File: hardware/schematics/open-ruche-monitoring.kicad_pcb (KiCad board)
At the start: 2 copper layers, 139.4 x 98.4 mm, 31 parts, among them J1 HX711, J10 MMA8451, J11 CONN_LIPO, J12 CONN_ALIM_ESP32, J2 DHT22_EXT, J3 DHT22_INT, J4 SONDE_TEMP_1, J5 SONDE_TEMP_2, J6 Light Sensor, J7 LORA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

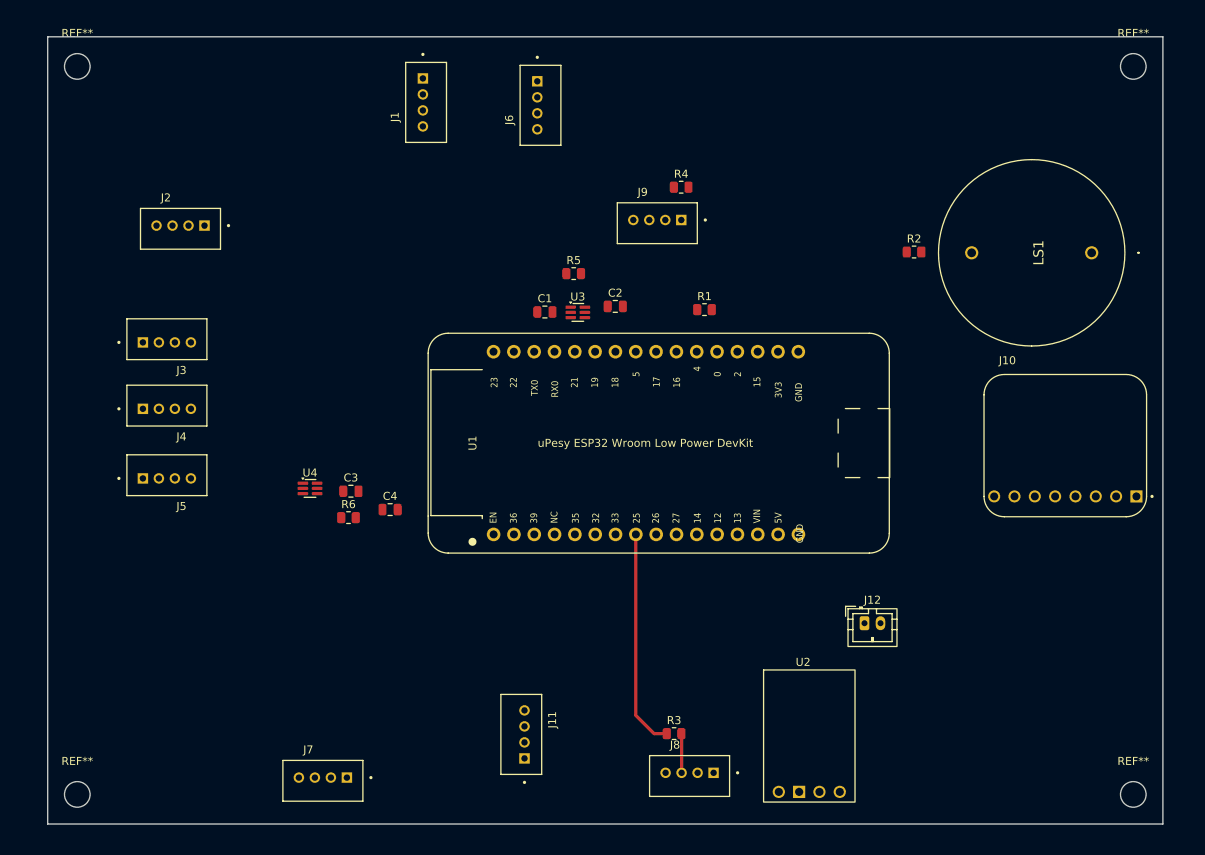
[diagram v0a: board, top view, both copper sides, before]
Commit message: hw(3D) Add 3D models for lora, hx711 and lipo charger
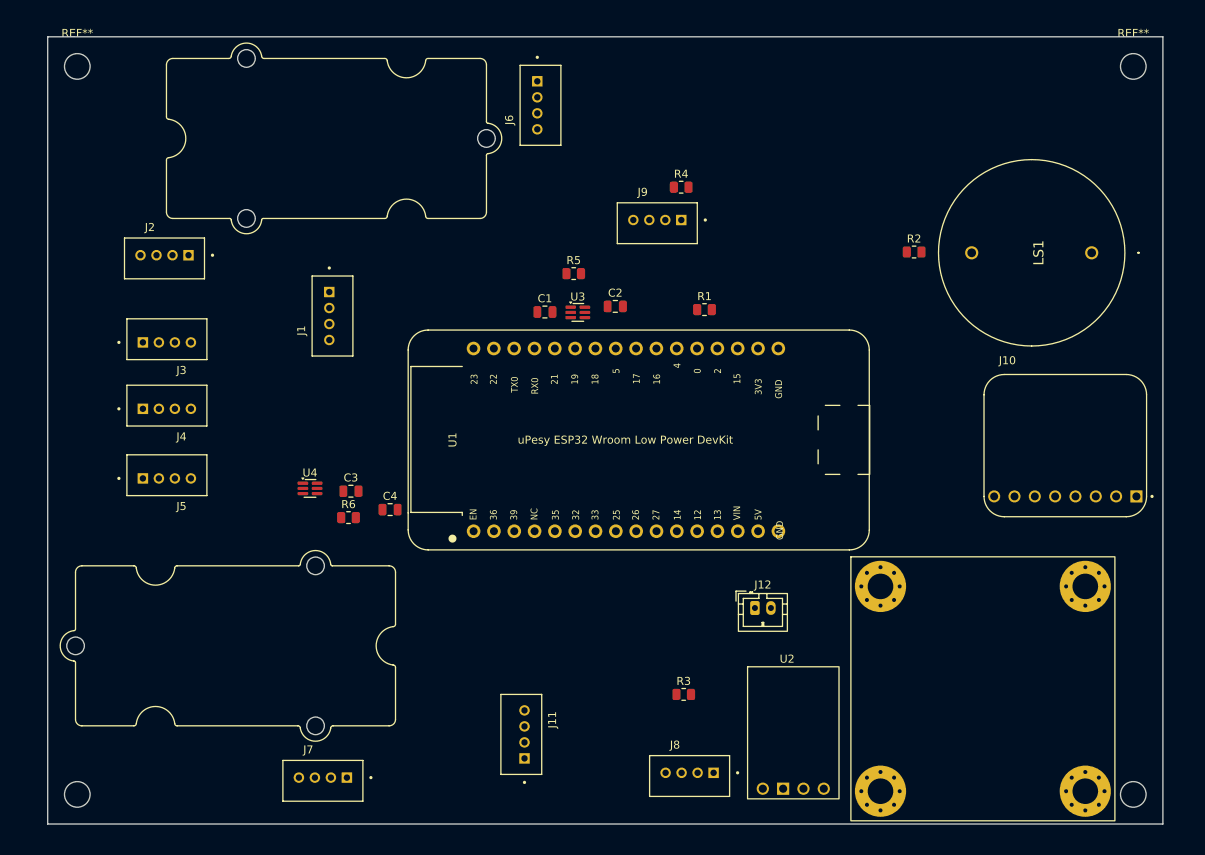
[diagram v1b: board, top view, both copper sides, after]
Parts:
- added REF**: DFR0264, lipo_charger:DFR0264, F.Cu at (197.9, 125.9)
- added REF**: hx711_module, hx711_grove:hx711_module, F.Cu at (98.5, 55.7)
- added REF**: lora_module, lora_grove:lora_module, F.Cu at (105.5, 126.8)
- U1: value uPesy_ESP32_Wroom_Low_Power_DevKit -> uPesy ESP32 Wroom Low Power DevKit
- moved J1 29.2 mm to (117.0, 77.9)
- moved J12 13.8 mm to (170.2, 114.4)
- moved R3 5.04 mm to (161.3, 125.2)
- moved J2 4.21 mm to (96.4, 70.3)
- moved U1 2.53 mm to (154.0, 93.5)
- moved U2 2.04 mm to (175.0, 130.0)
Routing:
- net /TX_XIAO: track 27.4 -> 0.00 mm
- net Net-(J8-SIG1): track 4.91 -> 0.00 mm

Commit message: hw(pcb) save pcb to try another layout
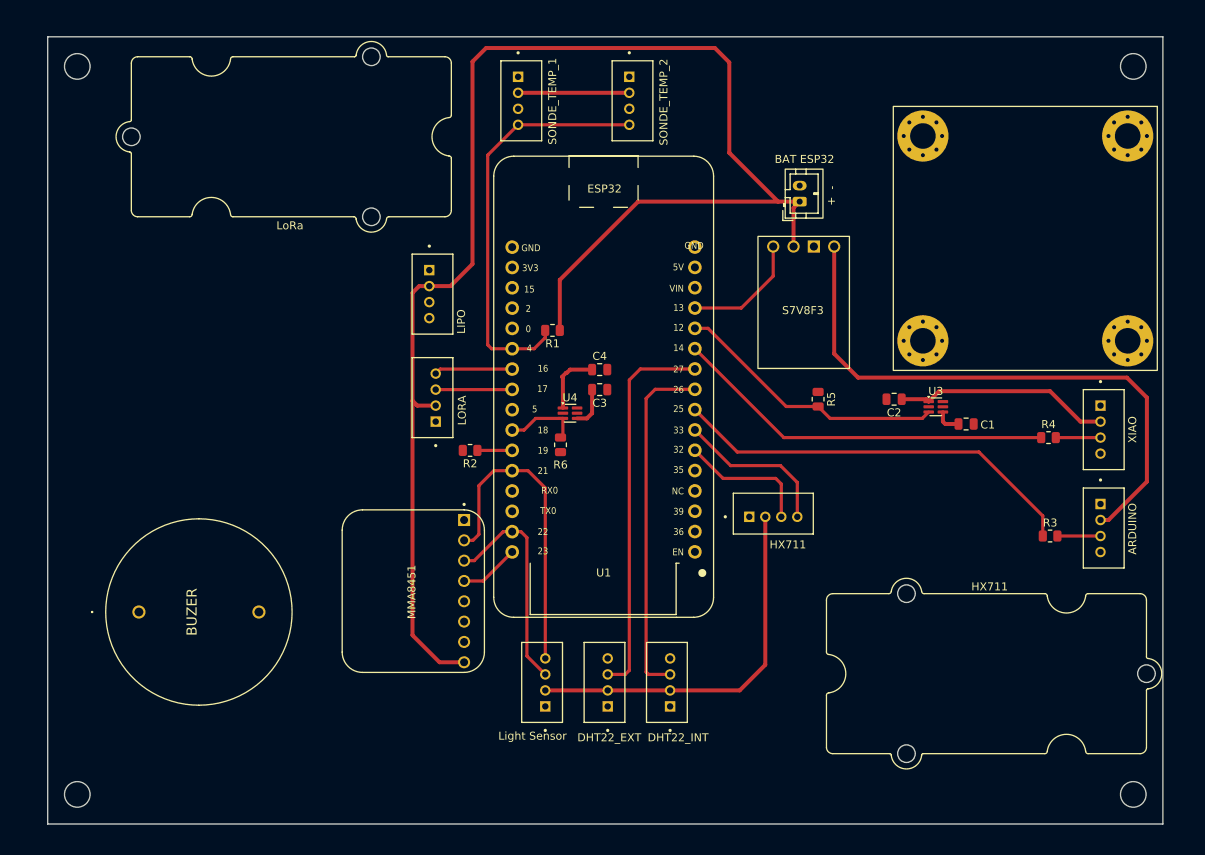
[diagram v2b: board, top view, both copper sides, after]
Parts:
- BAT ESP32: renamed from J12
- J11: value CONN_LIPO -> LIPO
- REF**: value lora_module -> LoRa
- U1: value uPesy ESP32 Wroom Low Power DevKit -> uPesy_ESP32_Wroom_Low_Power_DevKit
- U2: value 3.3V-STEP-DOWN_VOLTAGE_REGULATOR_S7V8F3 -> S7V8F3
- moved BUZER 127.3 mm to (93.2, 114.9), turned to -90 degrees
- moved REF** 106.2 mm to (181.0, 122.6)
- moved J10 83.5 mm to (127.5, 112.3), turned to 90 degrees
- moved J2 76.9 mm to (151.8, 123.7), turned to -90 degrees
- moved J3 75.9 mm to (159.6, 123.7), turned to -90 degrees
- moved J5 74.6 mm to (154.5, 51.0), turned to 90 degrees
- moved J6 72.1 mm to (144.0, 123.7), turned to -90 degrees
- moved REF** 64.0 mm to (112.5, 63.2)
- moved XIAO 61.3 mm to (213.4, 92.1), turned to 90 degrees
- moved HX711 60.9 mm to (172.5, 103.0), turned to 180 degrees
- moved R2 60.8 mm to (134.6, 94.7), turned to 180 degrees
- moved ARDUINO 59.8 mm to (213.4, 104.4), turned to 90 degrees
- moved REF** 58.7 mm to (202.6, 67.4), turned to -90 degrees
- moved J4 58.4 mm to (140.6, 51.0), turned to 90 degrees
- moved J11 56.3 mm to (129.5, 75.2), turned to 90 degrees
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- renumbered J8 to ARDUINO, LS1 to BUZER, J1 to HX711, J9 to XIAO
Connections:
- U1 pad 12: /EN_SENSORS -> /EN_XIAO
- U1 pad 23: /EN_XIAO -> /EN_SENSORS
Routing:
- net /+3.7V: track 0.00 -> 196.2 mm
- net /LS_ARDUINO_OUT: track 0.00 -> 73.0 mm
- net /LS_SENSORS_OUT: track 0.00 -> 69.3 mm
- net /ONE_WIRE_TEMP: track 0.00 -> 51.8 mm
- net /TX_XIAO: track 0.00 -> 51.5 mm
- net /DATA_DHT22_EXT: track 0.00 -> 48.0 mm
- net /TX_ARDUINO: track 0.00 -> 47.9 mm
- net /DATA_DHT22_INT: track 0.11 -> 44.0 mm
- net /SDA: track 0.00 -> 39.5 mm
- net /EN_XIAO: track 0.00 -> 34.2 mm
- net /SCL: track 0.00 -> 27.7 mm
- net /LS_XIAO_OUT: track 0.00 -> 27.1 mm
- net /PSCK: track 0.00 -> 19.8 mm
- net /DOUT: track 0.00 -> 16.6 mm
- net /EN_ARDUINO: track 0.00 -> 15.1 mm
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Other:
- board text added: "+"
- board text added: "-"

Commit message: hw(pcb) pcb done
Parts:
- removed ARDUINO: CONN_ARDUINO, Grove:SEEED_110990030
- removed BAT ESP32: CONN_ALIM_ESP32, Connector_JST:JST_PH_B2B-PH-K_1x02_P2.00mm_Vertical
- removed BUZER: KPEG222, KPEG222:KPEG222
- removed C1, C3: 1u, Capacitor_SMD:C_0805_2012Metric
- removed C2, C4: 0.1u, Capacitor_SMD:C_0805_2012Metric
- removed HX711: HX711, Grove:SEEED_110990030
- removed R5, R6: 20k, Resistor_SMD:R_0805_2012Metric
- removed the REF** at (202.6, 67.4)
- removed the REF** at (112.5, 63.2)
- removed U4: SiP32431DR3, Package_TO_SOT_SMD:SOT-363_SC-70-6
- removed XIAO: CONN_XIAO, Grove:SEEED_110990030
- added BAT: lipo_bat, battery:lipo_bat, F.Cu at (106.3, 95.9)
- added BUZZER: KPEG222, KPEG222:KPEG222, F.Cu at (213.4, 93.9)
- added J1: HX711, Grove:SEEED_110990030, F.Cu at (156.9, 64.3)
- added J12: BAT ESP32, Connector_JST:JST_PH_B2B-PH-K_1x02_P2.00mm_Vertical, F.Cu at (125.4, 60.2)
- added J8: ARDUINO, Grove:SEEED_110990030, F.Cu at (182.6, 75.4)
- added J9: XIAO, Grove:SEEED_110990030, F.Cu at (189.0, 75.3)
- added LIPO_CHARGER: LIPO CHARGER, lipo_charger:DFR0264, F.Cu at (103.9, 67.0)
- added LORA: lora_module, lora_grove:lora_module, F.Cu at (198.8, 113.3)
- J11: value LIPO -> CONN ALIM
- J6: value Light Sensor -> LUX
- R1, R2, R3, R4: footprint Resistor_SMD:R_0805_2012Metric -> Resistor_THT:R_Axial_DIN0207_L6.3mm_D2.5mm_P10.16mm_Horizontal
- U1: value uPesy_ESP32_Wroom_Low_Power_DevKit -> uPesy ESP32 Wroom Low Power DevKit
- U3: value SiP32431DR3 -> S7V8F5; footprint Package_TO_SOT_SMD:SOT-363_SC-70-6 -> Pololu:MODULE_STEP-DOWN_VOLTAGE_REGULATOR_D24V6F3
- moved R3 67.5 mm to (145.7, 77.2)
- moved REF** 67.1 mm to (174.4, 55.8)
- moved J5 64.0 mm to (133.1, 111.3), turned to -90 degrees
- moved J4 60.3 mm to (141.8, 111.3), turned to -90 degrees
- moved J3 60.1 mm to (150.5, 64.3), turned to 90 degrees
- moved J2 59.9 mm to (143.8, 64.3), turned to 90 degrees
- moved U3 57.6 mm to (150.4, 50.3), turned to -90 degrees
- moved R4 54.9 mm to (153.5, 80.4)
- moved R2 46.8 mm to (181.3, 92.1), turned to 0 degrees
- moved U2 43.9 mm to (135.1, 61.1)
- moved J10 40.0 mm to (167.2, 107.2), turned to 180 degrees
- moved J7 30.8 mm to (150.6, 111.3)
- moved J11 26.6 mm to (125.1, 48.9), turned to 0 degrees
- moved R1 22.0 mm to (135.6, 99.6), turned to 0 degrees
- moved J6 18.5 mm to (161.9, 119.2), turned to 0 degrees
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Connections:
- J10 pad 1: GND -> unconnected-(J10-Pin_1-Pad1)
- J10 pad 8: /+3.7V -> /+3.3V
- J2 pad 2: /LS_SENSORS_OUT -> /+3.3V_REG
- J3 pad 2: /LS_SENSORS_OUT -> /+3.3V_REG
- J4 pad 2: /LS_SENSORS_OUT -> /+3.3V_REG
- J5 pad 2: /LS_SENSORS_OUT -> /+3.3V_REG
- J6 pad 2: /LS_SENSORS_OUT -> /+3.3V_REG
- J7 pad 2: /+3.7V -> /+3.3V_REG
- R1 pad 1: /+3.7V -> /+3.3V
- R3 pad 1: /TX_XIAO -> /TX_ARDUINO
- R4 pad 1: /TX_ARDUINO -> /TX_XIAO
- U1 pad 12: /EN_XIAO -> /EN_3.3V_REG
- U1 pad 13: /EN_ARDUINO -> /EN_5V_REG
- U1 pad 23: /EN_SENSORS -> unconnected-(U1-GPIO18-Pad23)
- U1 pad 31: unconnected-(U1-3V3-Pad31) -> /+3.3V
- U2 pad !SHDN: /EN_ARDUINO -> /EN_3.3V_REG
- U2 pad VOUT: /LS_ARDUINO_OUT -> /+3.3V_REG
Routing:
- net /+3.7V: track 196.2 -> 32.4 mm
- net /+3.3V_REG: track 0.00 -> 130.5 mm, vias 0 -> 1
- net /LS_ARDUINO_OUT: track 73.0 -> 0.00 mm
- net /+3.3V: track 0.00 -> 72.3 mm
- net /LS_SENSORS_OUT: track 69.3 -> 0.00 mm
- net /+5V_REG: track 0.00 -> 57.2 mm
- net /TX_XIAO: track 51.5 -> 8.01 mm
- net /TX_ARDUINO: track 47.9 -> 4.73 mm
- net /DATA_DHT22_EXT: track 48.0 -> 9.01 mm
- net /DATA_DHT22_INT: track 44.0 -> 9.40 mm
- net /EN_XIAO: track 34.2 -> 0.00 mm
- net /ONE_WIRE_TEMP: track 51.8 -> 23.3 mm
- net /LS_XIAO_OUT: track 27.1 -> 0.00 mm
- net /EN_5V_REG: track 0.00 -> 25.3 mm, vias 0 -> 1
- net /EN_3.3V_REG: track 0.00 -> 23.3 mm
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- added copper zone on B.Cu, net GND
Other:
- board text removed: "+"
- board text removed: "-"
